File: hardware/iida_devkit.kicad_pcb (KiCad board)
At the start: 4 copper layers, 261 parts, among them J1001 132134, J201 USB4105-GF-A, J202 PRPC001DAAN-RC, J301 B2B-XH-A, J302 PRPC001DAAN-RC, J401 61300111121, J402 PRPC001DAAN-RC, J403 PRPC001DAAN-RC, J404 PRPC001DAAN-RC, J501 PRPC006SAAN-RC, J502 TC2050, J503 61300611121, J504 61300611121, J505 61300611121, J506 61300611121, J507 61300611121, J508 PRPC001DAAN-RC, J509 PRPC006SAAN-RC, J901 SIM8066-6-1-14-01-A, Q301 IRLML6401TRPBF, Q302 DMN2005, Q303 DMN2005, Q501 BSS806NH, Q801 BSS806NH, Q802 IRLML6401TRPBF, Q803 BSS806NH, Q804 BSS806NH, Q805 BSS806NH, U201 USBLC6-2SC6, U301 BQ29728DSER, U302 MCP73833T-FCI/MF, U303 MAX17048G+T10, U401 LM66200DRLR, U402 TPS63020DSJR, U501 STM32L552CEU6, U502 AT25SF081B-MAHB-T, U601 MCP9808T-E/MC, U602 SHT40-AD1B-R2, U701 TCA9554PW, U801 SN74AVC4T774, U802 SARA-R500S-01B, Y501 ECS-160-9-37-CKM-TR3, Y502 ABS05-32.768KHZ-9-T

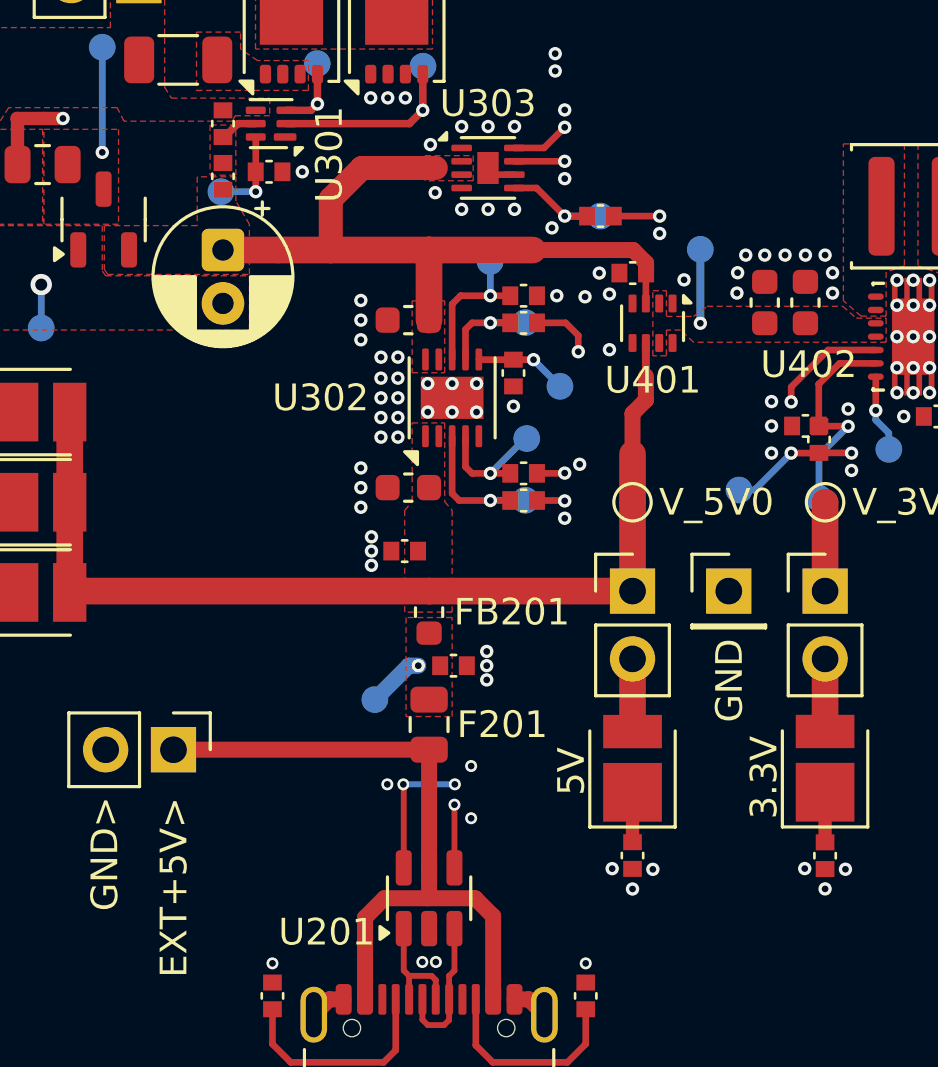
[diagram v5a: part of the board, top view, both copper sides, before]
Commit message: HW: Add power OR input caps
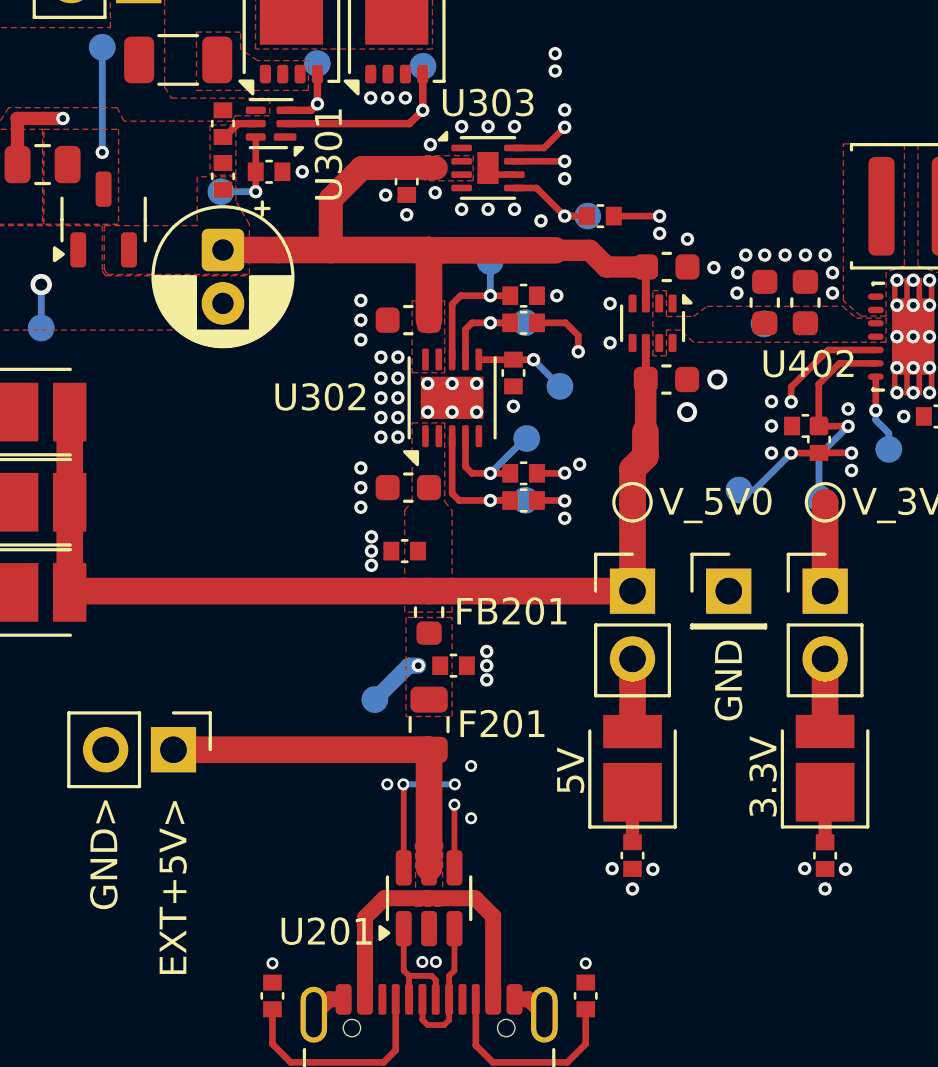
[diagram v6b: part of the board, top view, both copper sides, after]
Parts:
- added C401: 4.7 µF, Capacitor_SMD:C_0603_1608Metric, F.Cu at (71.7, 86.7)
- added C402: 4.7 µF, Capacitor_SMD:C_0603_1608Metric, F.Cu at (71.7, 82.5)
- moved C305 9.13 mm to (62.0, 79.3), turned to -90 degrees
- moved TP401 3.68 mm to (75.4, 84.6)
- moved TP313 0.47 mm to (68.7, 80.6)
- renumbered C401 to C403, C402 to C404, C403 to C405, C404 to C406, C405 to C407, C406 to C408
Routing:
- net /Power/V_SYS: track 2.77 -> 0.00 mm, vias 1 -> 0
- net /USB/VBUS: track 27.3 -> 26.2 mm
- net GND: vias 110 -> 113
- added copper zone on F.Cu, net /USB/VBUS

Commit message: HW: Add power pours and refactor power layout
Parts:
- U402: footprint Texas Instruments:TPS63021DSJR -> Texas Instruments:TPS6302xDSJ
- moved R304 0.32 mm to (66.3, 83.3)
- moved TP308 0.32 mm to (65.1, 82.0)
- moved R306 0.12 mm to (66.3, 91.4)
- moved TP310 0.12 mm to (66.4, 91.3)
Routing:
- net GND: vias 113 -> 124
- net /USB/VBUS_UNFILTERED: vias 4 -> 1
- added copper zone on B.Cu, net GND
- added copper zone on F.Cu, net GND
- added copper zone on In1.Cu, net V_3V3
- added copper zone on In2.Cu, net V_3V3

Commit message: HW: Layout sensors and IO expander
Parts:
- TP601, TP701: moved to B.Cu
- moved TP701 339.1 mm to (90.1, 160.0)
- moved TP601 325.4 mm to (88.8, 147.6), turned to 90 degrees
- moved R705 220.0 mm to (93.9, 164.0), turned to -90 degrees
- moved R708 219.8 mm to (76.0, 165.9), turned to 90 degrees
- moved R707 218.4 mm to (76.0, 162.5), turned to 90 degrees
- moved D701 217.3 mm to (73.2, 159.7), turned to 180 degrees
- moved R706 217.1 mm to (76.0, 159.2), turned to 90 degrees
- moved D702 216.4 mm to (73.2, 163.1), turned to 180 degrees
- moved D703 215.4 mm to (73.2, 166.4), turned to 180 degrees
- moved R703 214.7 mm to (82.6, 163.0), turned to -90 degrees
- moved R701 214.2 mm to (93.6, 160.4), turned to 90 degrees
- moved C701 213.5 mm to (91.6, 157.5), turned to 90 degrees
- moved R709 213.1 mm to (86.9, 163.6)
- moved R704 212.0 mm to (92.4, 164.0), turned to -90 degrees
- moved R702 211.9 mm to (92.1, 159.9), turned to 180 degrees
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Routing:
- net /Battery/BAT_MON_INTn: track 1.72 -> 63.0 mm, vias 1 -> 4
- net /Battery/I2C_SCL: track 1.89 -> 60.9 mm, vias 1 -> 6
- net /Battery/I2C_SDA: track 2.21 -> 57.1 mm, vias 1 -> 4
- net /IO expander/TEMP_INTn: track 0.00 -> 22.1 mm, vias 0 -> 2
- net /Microcontroller/USB_DP: track 2.37 -> 19.8 mm
- net /Microcontroller/USB_DN: track 6.63 -> 24.0 mm
- net /IO expander/LED_C: track 0.00 -> 10.1 mm, vias 0 -> 2
- net /IO expander/LED_B: track 0.00 -> 8.98 mm, vias 0 -> 2
- net /IO expander/LED_A: track 0.00 -> 8.90 mm, vias 0 -> 2
- net V_3V3: track 3.33 -> 9.31 mm, vias 12 -> 30
- net Net-(U701-P5): track 0.00 -> 4.49 mm
- net /IO expander/INTn: track 0.00 -> 4.16 mm, vias 0 -> 1
- net /Sensors/TEMP_ALERT: track 0.00 -> 3.90 mm, vias 0 -> 1
- net Net-(U701-P4): track 0.00 -> 2.67 mm
- net Net-(U701-P3): track 0.00 -> 2.03 mm
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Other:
- board text added: "A"
- board text added: "B"
- board text added: "C"
- board text added: "IO_EXP_INTn"
- board text added: "TEMP_ALERT"
